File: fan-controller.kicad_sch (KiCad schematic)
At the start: 22 parts, among them J8 Molex_KK_1x4_0470531000, U14 MAX31740ATA+T, U6 LP2985IM5X-5.0_SOT

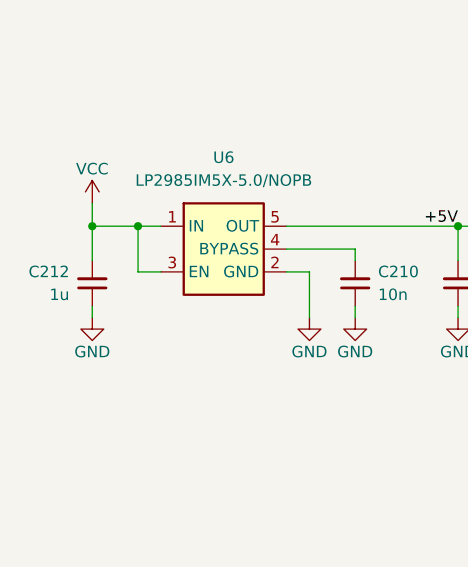
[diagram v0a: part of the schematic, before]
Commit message: [#91871] Change LEDs resistors from 10k to 1k, minor BOM consolidation
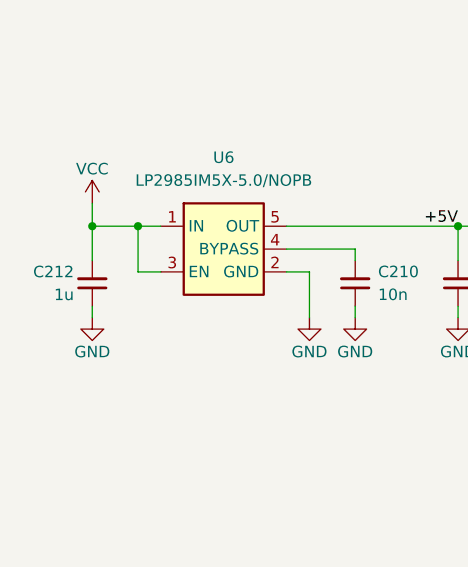
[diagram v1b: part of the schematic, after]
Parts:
- removed C212: C_1u_16V_X7R_0603, antmicro-footprints:C_0603_1608Metric, symbol antmicroCapacitors0603:C_1u_16V_X7R_0603
- added C212: C_1u_25V_0402, antmicro-footprints:C_0402_1005Metric, symbol antmicroCapacitors0402:C_1u_25V_0402
- C209: value C_1u_0402 -> C_1u_25V_0402; symbol antmicroCapacitors0402:C_1u_0402 -> antmicroCapacitors0402:C_1u_25V_0402; Dielectric (none) -> X5R; MPN C1005X6S1A105K050BC -> GRM155R61E105KE11J; Manufacturer TDK -> Murata; Voltage (none) -> 25V
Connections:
- net GND: now also C212.1
- net VCC: now also C212.2
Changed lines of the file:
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@@
 	)
 	(symbol
+		(lib_id "antmicroCapacitors0402:C_1u_25V_0402")
+		(at 54.61 149.86 270)
+		(mirror x)
+		(unit 1)
+		(exclude_from_sim no)
+		(in_bom yes)
+		(on_board yes)
+		(dnp no)
+		(property "Reference" "C212"
+			(at 52.578 146.05 90)
+			(effects
+				(font
+					(size 1.27 1.27)
+					(thickness 0.15)
+				)
+				(justify right)
+			)
+		)
+		(property "Value" "C_1u_25V_0402"
+			(at 44.45 129.54 0)
+			(effects
+				(font
+					(size 1.27 1.27)
+					(thickness 0.15)
+				)
+				(justify left bottom)
+				(hide yes)
+			)
+		)
+		(property "Footprint" "antmicro-footprints:C_0402_1005Metric"
+			(at 41.91 129.54 0)
+			(effects
+				(font
+					(size 1.27 1.27)
+					(thickness 0.15)
+				)
+				(justify left bottom)
+				(hide yes)
+			)
+		)
+		(property "Datasheet" "https://www.murata.com/products/productdetail?partno=GRM155R61E105KE11%23"
+			(at 39.37 129.54 0)
+			(effects
+				(font
+					(size 1.27 1.27)
+					(thickness 0.15)
+				)
+				(justify left bottom)
+				(hide yes)
+			)
+		)
+		(property "Description" "SMD Multilayer Ceramic Capacitor, 1 µF, 25 V, 0402 [1005 Metric], ± 10%, X5R, GRM Series"
+			(at 21.59 129.54 0)
+			(effects
+				(font
+					(size 1.27 1.27)
+				)
+				(justify left bottom)
+				(hide yes)
+			)
+		)
+		(property "MPN" "GRM155R61E105KE11J"
+			(at 36.83 129.54 0)
+			(effects
+				(font
+					(size 1.27 1.27)
+					(thickness 0.15)
+				)
+				(justify left bottom)
+				(hide yes)
+			)
+		)
+		(property "Manufacturer" "Murata"
+			(at 34.29 129.54 0)
+			(effects
+				(font
+					(size 1.27 1.27)
+					(thickness 0.15)
+				)
+				(justify left bottom)
+				(hide yes)
+			)
+		)
+		(property "License" "Apache-2.0"
+			(at 31.75 129.54 0)
+			(effects
+				(font
+					(size 1.27 1.27)
+					(thickness 0.15)
+				)
+				(justify left bottom)
+				(hide yes)
+			)
+		)
+		(property "Author" "Antmicro"
+			(at 29.21 129.54 0)
+			(effects
+				(font
+					(size 1.27 1.27)
+					(thickness 0.15)
+				)
+				(justify left bottom)
+				(hide yes)
+			)
+		)
+		(property "Val" "1u"
+			(at 52.578 148.59 90)
+			(effects
+				(font
+					(size 1.27 1.27)
+					(thickness 0.15)
+				)
+				(justify right)
+			)
+		)
+		(property "Voltage" "25V"
+			(at 26.67 129.54 0)
+			(effects
+				(font
+					(size 1.27 1.27)
+				)
+				(justify left bottom)
+				(hide yes)
+			)
+		)
+		(property "Dielectric" "X5R"
+			(at 24.13 129.54 0)
+			(effects
+				(font
+					(size 1.27 1.27)
+				)
+				(justify left bottom)
+				(hide yes)
+			)
+		)
+		(pin "1"
+		)
+		(pin "2"
+		)
+		(instances
+			(project "oculink-to-10gbe-adapter"
+				(path "/04bda987-e5eb-48b4-9e90-d8211dc11b39/cfdaa22c-cb6e-476e-82f5-94f72ae97682"
+					(reference "C212")
+					(unit 1)
+				)
+			)
+		)
+	)
+	(symbol
 		(lib_id "antmicroTVSDiodes:SZSMF4L14AT3G")
 		(at 322.58 133.35 90)
@@
 	)
 	(symbol
-		(lib_id "antmicroCapacitors0402:C_1u_0402")
+		(lib_id "antmicroCapacitors0402:C_1u_25V_0402")
 		(at 172.72 144.78 90)
 		(unit 1)
@@
 			)
 		)
-		(property "Value" "C_1u_0402"
+		(property "Value" "C_1u_25V_0402"
 			(at 182.88 124.46 0)
 			(effects
@@
 			)
 		)
-		(property "Datasheet" "https://product.tdk.com/en/search/capacitor/ceramic/mlcc/info?part_no=C1005X6S1A105K050BC"
+		(property "Datasheet" "https://www.murata.com/products/productdetail?partno=GRM155R61E105KE11%23"
 			(at 187.96 124.46 0)
 			(effects
@@
 			)
 		)
-		(property "Description" "SMD Multilayer Ceramic Capacitor, 1 µF, 10 V, 0402 [1005 Metric], ± 10%, X6S, C"
+		(property "Description" "SMD Multilayer Ceramic Capacitor, 1 µF, 25 V, 0402 [1005 Metric], ± 10%, X5R, GRM Series"
 			(at 205.74 124.46 0)
 			(effects
@@
 			)
 		)
-		(property "MPN" "C1005X6S1A105K050BC"
+		(property "MPN" "GRM155R61E105KE11J"
 			(at 190.5 124.46 0)
 			(effects
@@
 			)
 		)
-		(property "Manufacturer" "TDK"
+		(property "Manufacturer" "Murata"
 			(at 193.04 124.46 0)
 			(effects
@@
 			)
 		)
-		(property "Voltage" ""
+		(property "Voltage" "25V"
 			(at 200.66 124.46 0)
 			(effects
@@
 			)
 		)
-		(property "Dielectric" ""
+		(property "Dielectric" "X5R"
 			(at 203.2 124.46 0)
 			(effects
@@
 					(unit 1)
 				)
-			)
-		)
-	)
-	(symbol
-		(lib_id "antmicroCapacitors0603:C_1u_16V_X7R_0603")
-		(at 54.61 149.86 90)
-		(unit 1)
-		(exclude_from_sim no)
-		(in_bom yes)
-		(on_board yes)
-		(dnp no)
-		(property "Reference" "C212"
-			(at 52.07 146.0436 90)
-			(effects
-				(font
-					(size 1.27 1.27)
-					(thickness 0.15)
-				)
-				(justify left)
-			)
-		)
-		(property "Value" "C_1u_16V_X7R_0603"
-			(at 64.77 134.62 0)
-			(effects
-				(font
-					(size 1.27 1.27)
-					(thickness 0.15)
-				)
-				(justify left bottom)
-				(hide yes)
-			)
-		)
-		(property "Footprint" "antmicro-footprints:C_0603_1608Metric"
-			(at 67.31 134.62 0)
-			(effects
-				(font
-					(size 1.27 1.27)
-					(thickness 0.15)
-				)
-				(justify left bottom)
-				(hide yes)
-			)
-		)
-		(property "Datasheet" "https://www.kemet.com/en/us/capacitors/product/C0603C105K4RAC7411.html"
-			(at 69.85 134.62 0)
-			(effects
-				(font
-					(size 1.27 1.27)
-					(thickness 0.15)
-				)
-				(justify left bottom)
-				(hide yes)
-			)
-		)
-		(property "Description" "SMD Multilayer Ceramic Capacitor, 1µF, 16V, 0603, ±10%, X7R"
-			(at 87.63 134.62 0)
-			(effects
-				(font
-					(size 1.27 1.27)
-				)
-				(justify left bottom)
-				(hide yes)
-			)
-		)
-		(property "MPN" "C0603C105K4RAC7411"
-			(at 72.39 134.62 0)
-			(effects
-				(font
-					(size 1.27 1.27)
-					(thickness 0.15)
-				)
-				(justify left bottom)
-				(hide yes)
-			)
-		)
-		(property "Val" "1u"
-			(at 52.07 148.5836 90)
-			(effects
-				(font
-					(size 1.27 1.27)
-					(thickness 0.15)
-				)
-				(justify left)
-			)
-		)
-		(property "Voltage" "16V"
-			(at 74.93 134.62 0)
-			(effects
-				(font
-					(size 1.27 1.27)
-					(thickness 0.15)
-				)
-				(justify left bottom)
-				(hide yes)
-			)
-		)
-		(property "Dielectric" "X7R"
-			(at 77.47 134.62 0)
-			(effects
-				(font
-					(size 1.27 1.27)
-					(thickness 0.15)
-				)
-				(justify left bottom)
-				(hide yes)
-			)
-		)
-		(property "Manufacturer" "KEMET"
-			(at 80.01 134.62 0)
-			(effects
-				(font
-					(size 1.27 1.27)
-					(thickness 0.15)
-				)
-				(justify left bottom)
-				(hide yes)
-			)
-		)
-		(property "License" "Apache-2.0"
-			(at 82.55 134.62 0)
-			(effects
-				(font
-					(size 1.27 1.27)
-					(thickness 0.15)
-				)
-				(justify left bottom)
-				(hide yes)
-			)
-		)
-		(property "Author" "Antmicro"
-			(at 85.09 134.62 0)
-			(effects
-				(font
-					(size 1.27 1.27)
-					(thickness 0.15)
-				)
-				(justify left bottom)
-				(hide yes)
-			)
-		)
-		(pin "1"
-		)
-		(pin "2"
-		)
-		(instances
-			(project ""
-				(path "/04bda987-e5eb-48b4-9e90-d8211dc11b39/cfdaa22c-cb6e-476e-82f5-94f72ae97682"
-					(reference "C212")
-					(unit 1)
-				)
